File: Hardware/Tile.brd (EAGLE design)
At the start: 1 part

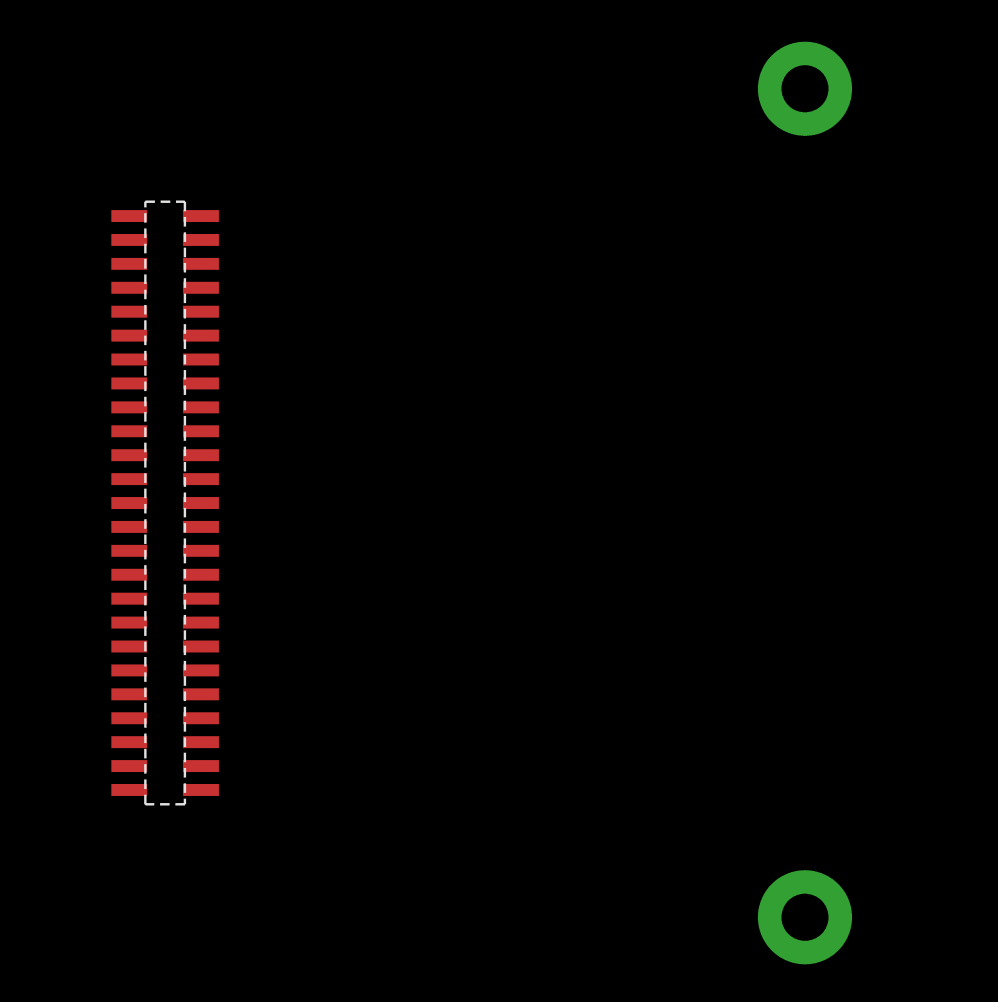
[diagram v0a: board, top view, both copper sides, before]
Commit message: Updated tile schematic and dimensions
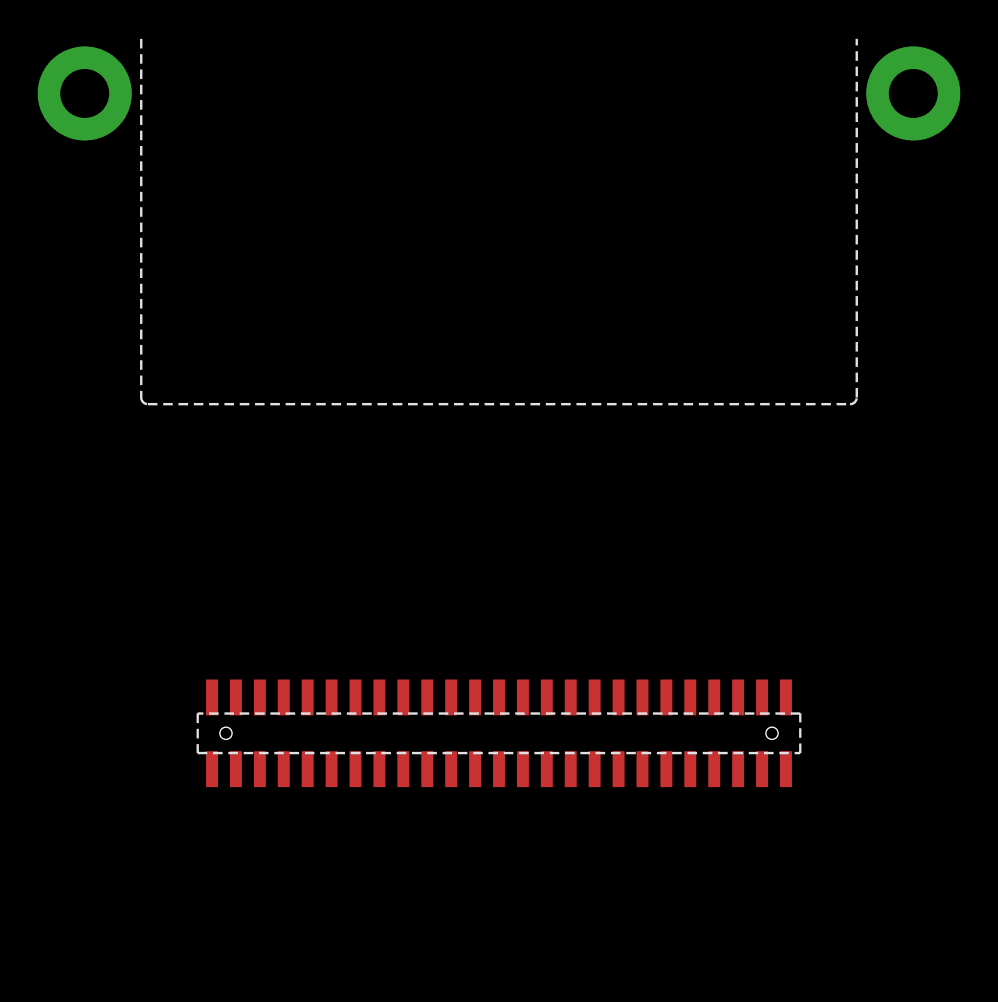
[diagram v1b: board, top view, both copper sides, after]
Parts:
- removed U$1: UTILE_LPCARRIER_SMD_MALE_1.27, amino:UTILE_LP
- added T1: UTILE_LPTILE, amino:UTILE_LP_T
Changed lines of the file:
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@@
 <setting verticaltext="up"/>
 </settings>
-<grid distance="1" unitdist="mm" unit="mm" style="lines" multiple="1" display="no" altdistance="0.025" altunitdist="inch" altunit="inch"/>
+<grid distance="1" unitdist="mm" unit="mm" style="lines" multiple="1" display="no" altdistance="0.02" altunitdist="mm" altunit="mm"/>
 <layers>
-<layer number="1" name="Top" color="4" fill="1" visible="yes" active="yes"/>
+<layer number="1" name="Top" color="30" fill="1" visible="yes" active="yes"/>
 <layer number="2" name="Route2" color="1" fill="3" visible="no" active="no"/>
 <layer number="3" name="Route3" color="4" fill="3" visible="no" active="no"/>
@@
 <layer number="15" name="Route15" color="4" fill="6" visible="no" active="no"/>
 <layer number="16" name="Bottom" color="1" fill="1" visible="yes" active="yes"/>
-<layer number="17" name="Pads" color="2" fill="1" visible="yes" active="yes"/>
+<layer number="17" name="Pads" color="30" fill="1" visible="yes" active="yes"/>
 <layer number="18" name="Vias" color="2" fill="1" visible="yes" active="yes"/>
 <layer number="19" name="Unrouted" color="6" fill="1" visible="yes" active="yes"/>
@@
 <layer number="48" name="Document" color="7" fill="1" visible="yes" active="yes"/>
 <layer number="49" name="Reference" color="7" fill="1" visible="yes" active="yes"/>
-<layer number="50" name="dxf" color="7" fill="1" visible="yes" active="yes"/>
+<layer number="50" name="dxf" color="7" fill="1" visible="no" active="no"/>
 <layer number="51" name="tDocu" color="7" fill="1" visible="yes" active="yes"/>
 <layer number="52" name="bDocu" color="7" fill="1" visible="yes" active="yes"/>
@@
 <layer number="89" name="SimProbes" color="9" fill="1" visible="yes" active="yes"/>
 <layer number="90" name="Modules" color="5" fill="1" visible="no" active="no"/>
-<layer number="91" name="Nets" color="2" fill="1" visible="no" active="no"/>
+<layer number="91" name="Nets" color="30" fill="1" visible="no" active="no"/>
 <layer number="92" name="Busses" color="1" fill="1" visible="no" active="no"/>
 <layer number="93" name="Pins" color="2" fill="1" visible="no" active="no"/>
-<layer number="94" name="Symbols" color="4" fill="1" visible="no" active="no"/>
+<layer number="94" name="Symbols" color="31" fill="1" visible="no" active="no"/>
 <layer number="95" name="Names" color="7" fill="1" visible="no" active="no"/>
 <layer number="96" name="Values" color="7" fill="1" visible="no" active="no"/>
@@
 <board>
 <plain>
-<dimension x1="44" y1="50" x2="44" y2="0" x3="54" y3="25" textsize="1.778" layer="21"/>
-<dimension x1="0" y1="49" x2="44" y2="49" x3="22" y3="60" textsize="1.778" layer="21"/>
-<dimension x1="0" y1="26" x2="7" y2="26" x3="3.5" y3="53" textsize="1.778" layer="21"/>
-<dimension x1="41" y1="47" x2="0" y2="47" x3="20.5" y3="56" textsize="1.778" layer="21"/>
-<dimension x1="41" y1="0" x2="41" y2="3" x3="47" y3="1.5" textsize="1.778" layer="21"/>
-<dimension x1="7" y1="25" x2="7" y2="0" x3="50" y3="12.5" textsize="1.778" layer="21"/>
+<dimension x1="0" y1="29" x2="49.5" y2="29" x3="24.75" y3="-7" textsize="1.778" layer="20" visible="yes"/>
+<dimension x1="10.75" y1="30.25" x2="10.75" y2="49.75" x3="54" y3="40" textsize="1.778" layer="20" visible="yes"/>
+<dimension x1="5.75" y1="41.25" x2="43.75" y2="41.25" x3="24.75" y3="52" textsize="1.778" layer="20" visible="yes"/>
+<dimension x1="0" y1="46.75" x2="2.75" y2="46.75" x3="1.375" y3="26" textsize="1.778" layer="20" visible="yes"/>
+<dimension x1="2.75" y1="49.75" x2="2.75" y2="46.75" x3="-2" y3="48.25" textsize="1.778" layer="20" width="0.26" visible="yes"/>
+<dimension x1="46.75" y1="48" x2="46.75" y2="45.5" x3="48" y3="46.75" textsize="1.778" layer="20" dtype="diameter" width="0.26" visible="yes"/>
+<dimension x1="37" y1="0" x2="37.75" y2="49.75" x3="64" y3="24.875" textsize="1.778" layer="20" dtype="vertical" width="0.26" visible="yes"/>
+<dimension x1="8.5" y1="49.75" x2="10.25" y2="12.75" x3="59" y3="31.25" textsize="1.778" layer="20" dtype="vertical" width="0.26" visible="yes"/>
 </plain>
 <attributes>
@@
 </autorouter>
 <elements>
-<element name="U$1" library="amino" package="UTILE_LP" value="UTILE_LPCARRIER_SMD_MALE_1.27" x="18.5" y="25"/>
+<element name="T1" library="amino" package="UTILE_LP_T" value="UTILE_LPTILE" x="24.75" y="24.25" rot="MR90"/>
 </elements>
 <signals>
